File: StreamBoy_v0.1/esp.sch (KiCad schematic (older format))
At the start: 9 parts, among them Q1 SS8050-G, Q2 SS8050-G

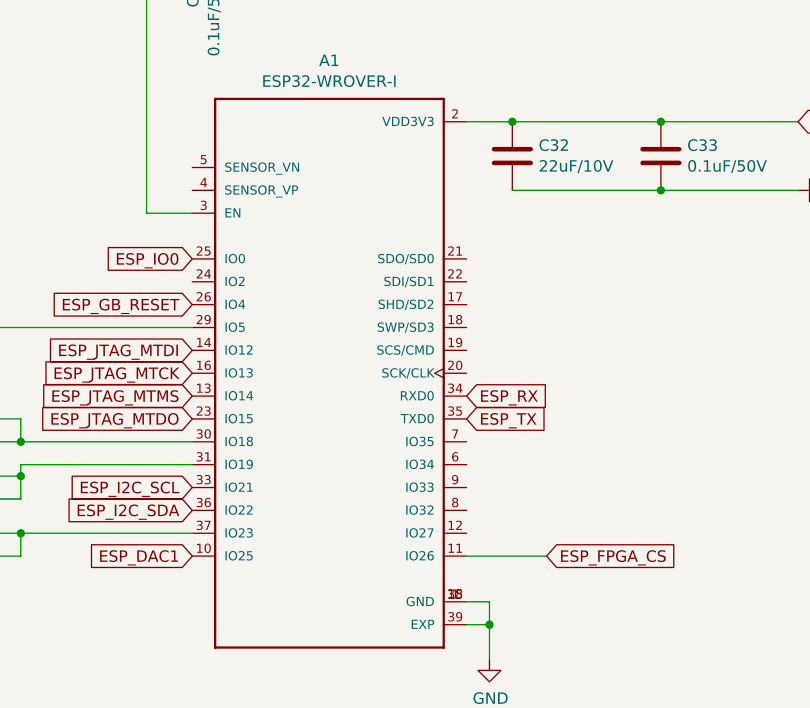
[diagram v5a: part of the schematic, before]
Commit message: Add leds and buttons to debug
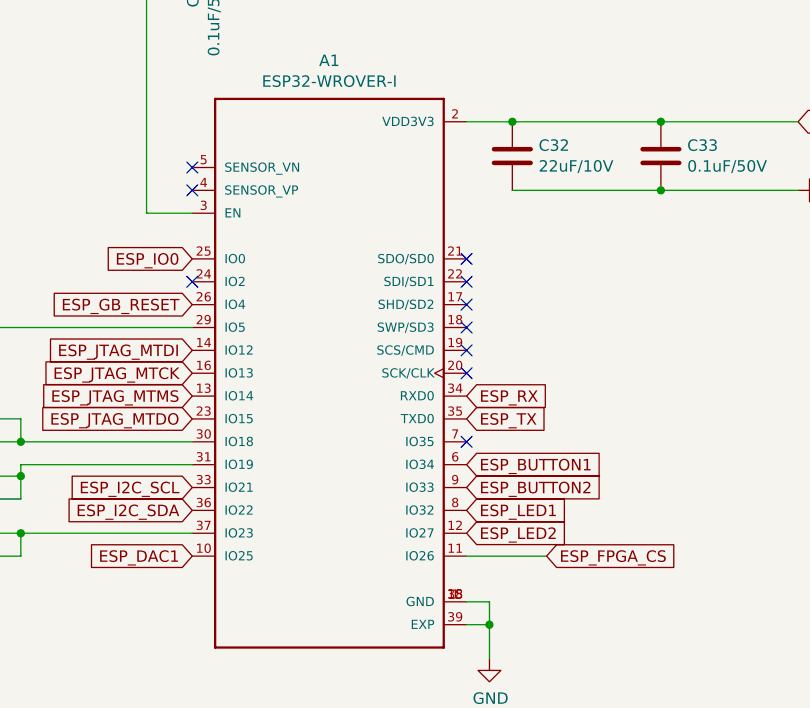
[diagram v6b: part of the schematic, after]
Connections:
- net ESP_LED2: now reaches A1.12 (IO27)
- net ESP_BUTTON1: now reaches A1.6 (IO34)
- net ESP_LED1: now reaches A1.8 (IO32)
- net ESP_BUTTON2: now reaches A1.9 (IO33)
- no-connect marks 0 -> 10
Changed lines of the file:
@@
 Wire Wire Line
 	1500 5900 1600 5900
+Text GLabel 3850 3750 2    50   Input ~ 0
+ESP_LED1
+Text GLabel 3850 3650 2    50   Input ~ 0
+ESP_BUTTON2
+Text GLabel 3850 3550 2    50   Input ~ 0
+ESP_BUTTON1
+Text GLabel 3850 3850 2    50   Input ~ 0
+ESP_LED2
+NoConn ~ 3850 3450
+NoConn ~ 3850 3150
+NoConn ~ 3850 3050
+NoConn ~ 3850 2950
+NoConn ~ 3850 2850
+NoConn ~ 3850 2750
+NoConn ~ 3850 2650
+NoConn ~ 2650 2250
+NoConn ~ 2650 2350
+NoConn ~ 2650 2750
 $EndSCHEMATC

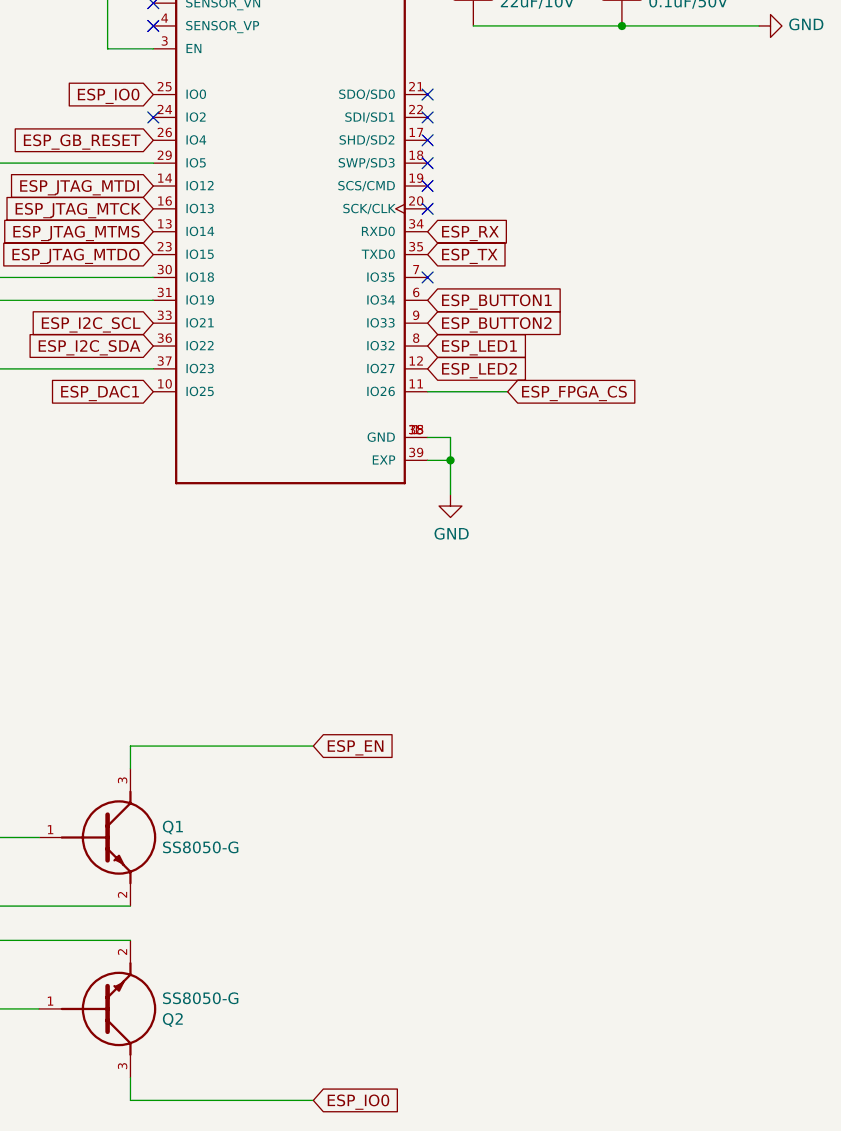
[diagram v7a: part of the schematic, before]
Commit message: GB Reset fixed and moved some stuff
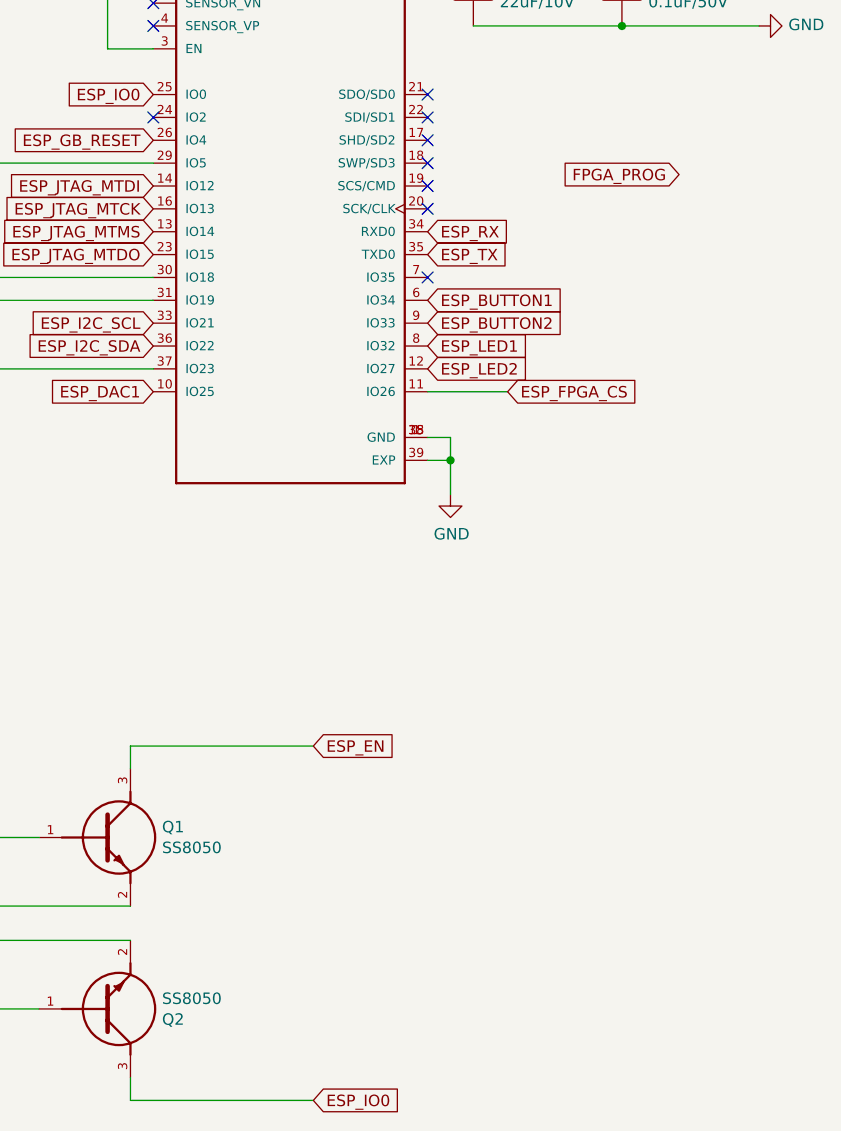
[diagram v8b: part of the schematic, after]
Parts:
- C31, C33: lcscPartnum (none) -> C15195
- Q1, Q2: value SS8050-G -> SS8050; Description (none) -> Replaced from ss8050-g; lcscPartnum (none) -> C2146
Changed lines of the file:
@@
 F 2 "Capacitor_SMD:C_0805_2012Metric" H 4738 2050 50  0001 C CNN
 F 3 "~" H 4700 2200 50  0001 C CNN
+F 4 "C15195" H 4700 2200 50  0001 C CNN "lcscPartnum"
 	1    4700 2200
 	1    0    0    -1
@@
 F 2 "Capacitor_SMD:C_0805_2012Metric" H 2738 1150 50  0001 C CNN
 F 3 "~" H 2700 1300 50  0001 C CNN
+F 4 "C15195" H 2700 1300 50  0001 C CNN "lcscPartnum"
 	1    2700 1300
 	0    -1   1    0
@@
 AR Path="/5E0FBAC6/5E15CB3B" Ref="Q1"  Part="1"
 F 0 "Q1" H 2688 5946 50  0000 L CNN
-F 1 "SS8050-G" H 2688 5855 50  0000 L CNN
+F 1 "SS8050" H 2688 5855 50  0000 L CNN
 F 2 "SOT95P240X115-3N" H 2150 5900 50  0001 L BNN
 F 3 "1.15mm" H 2150 5900 50  0001 L BNN
@@
 F 7 "" H 2150 5900 50  0001 L BNN "Field7"
 F 8 "SS8050-G" H 2150 5900 50  0001 L BNN "Field8"
+F 9 "Replaced from ss8050-g" H 2150 5900 50  0001 C CNN "Description"
+F 10 "C2146" H 2150 5900 50  0001 C CNN "lcscPartnum"
 	1    2150 5900
 	1    0    0    -1
@@
 AR Path="/5E0FBAC6/5E15CB46" Ref="Q2"  Part="1"
 F 0 "Q2" H 2688 6696 50  0000 L CNN
-F 1 "SS8050-G" H 2688 6605 50  0000 L CNN
+F 1 "SS8050" H 2688 6605 50  0000 L CNN
 F 2 "SOT95P240X115-3N" H 2150 6650 50  0001 L BNN
 F 3 "1.15mm" H 2150 6650 50  0001 L BNN
@@
 F 7 "" H 2150 6650 50  0001 L BNN "Field7"
 F 8 "SS8050-G" H 2150 6650 50  0001 L BNN "Field8"
+F 9 "Replaced from ss8050-g" H 2150 6650 50  0001 C CNN "Description"
+F 10 "C2146" H 2150 6650 50  0001 C CNN "lcscPartnum"
 	1    2150 6650
 	1    0    0    1
@@
 NoConn ~ 2650 2250
 NoConn ~ 2650 2350
+Text GLabel 4950 3000 0    50   Input ~ 0
+FPGA_PROG
 NoConn ~ 2650 2750
 $EndSCHEMATC
